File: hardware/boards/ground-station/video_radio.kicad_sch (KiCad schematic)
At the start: 7 parts, among them J5 U.FL, U11 TX5813

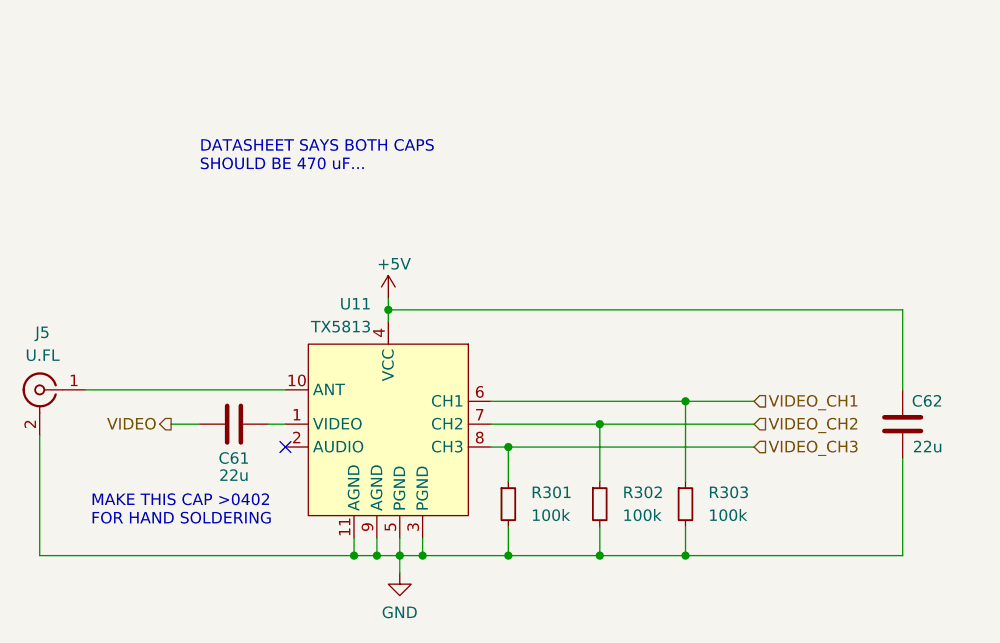
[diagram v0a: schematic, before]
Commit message: Updated video radio to RX5808
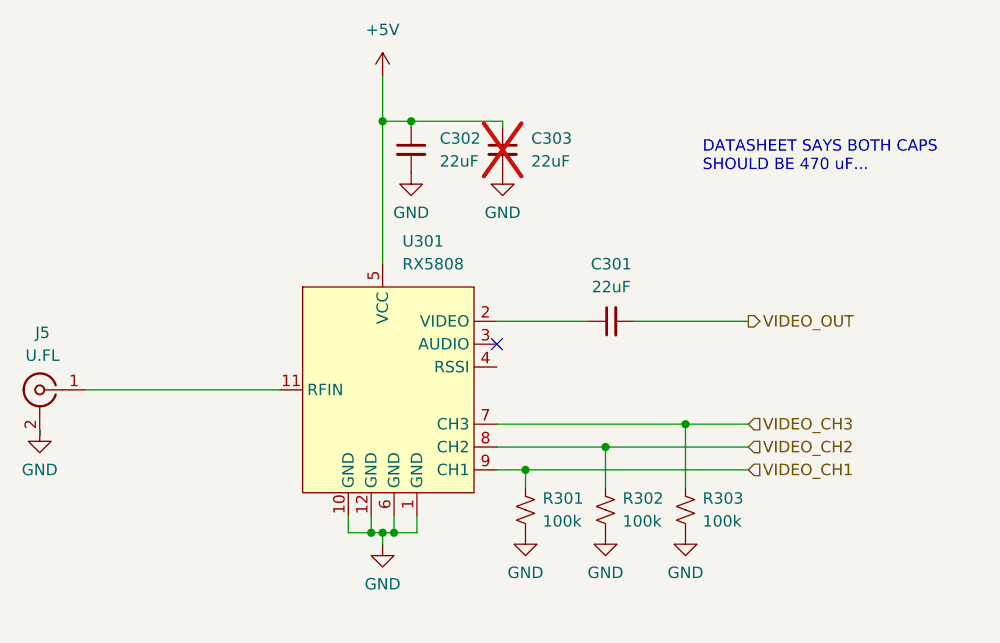
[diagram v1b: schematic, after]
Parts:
- removed C61: 22u, Capacitor_SMD:C_0603_1608Metric, symbol Device:C
- removed C62: 22u, Capacitor_SMD:C_0805_2012Metric, symbol Device:C
- removed R301, R302, R303: 100k, symbol Device:R_Small
- removed U11: TX5813, capstone:TX5813, symbol Capstone:TX5813
- added C301, C302, C303: 22uF, symbol Device:C_Small
- added R301, R302, R303: 100k, symbol Device:R_Small_US
- added U301: RX5808, symbol capstone:RX5808
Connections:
- net +5V: now also C302.1, C303.1, U301.5 (VCC)
- net GND: now also C302.2, C303.2, R301.2, R302.2, R303.2, U301.1 (GND), U301.10 (GND), U301.12 (GND), U301.6 (GND)
- net VIDEO_CH1: now also R301.1, U301.9 (CH1)
- net VIDEO_CH2: now also R302.1, U301.8 (CH2)
- net VIDEO_CH3: now also R303.1, U301.7 (CH3)
- net at J5.1 (In): now also U301.11 (RFIN)
- new net: C301.1, U301.2 (VIDEO)
- new net VIDEO_OUT: C301.2
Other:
- note removed: "MAKE THIS CAP >0402 FOR HAND SOLDERING"
